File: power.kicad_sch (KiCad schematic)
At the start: 19 parts, among them J7 Input, U1 U

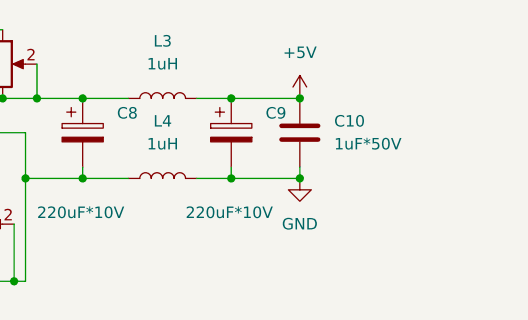
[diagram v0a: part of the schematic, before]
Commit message: Fix errors with LCD connection
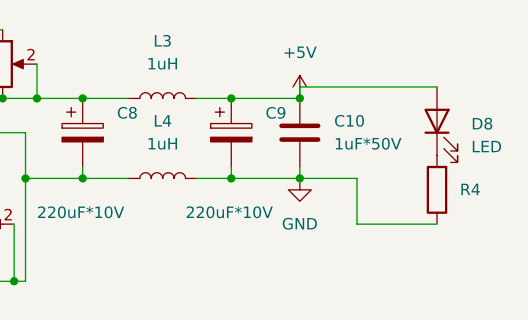
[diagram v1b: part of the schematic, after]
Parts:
- added D8: LED, LED_THT:LED_D3.0mm, symbol Device:LED
- added R4: 330, Resistor_SMD:R_1206_3216Metric_Pad1.30x1.75mm_HandSolder, symbol Device:R
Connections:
- net +5V: now also D8.2 (A)
- net GND: now also R4.1
- new net: D8.1 (K), R4.2
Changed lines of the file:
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@@
+	(wire
+		(pts
+			(xy 251.46 50.8) (xy 251.46 52.07)
+		)
+		(stroke
+			(width 0)
+			(type default)
+		)
+	)
 	(wire
 		(pts
@@
 	(wire
 		(pts
+			(xy 257.81 66.04) (xy 257.81 60.96)
+		)
+		(stroke
+			(width 0)
+			(type default)
+		)
+	)
+	(wire
+		(pts
 			(xy 222.25 48.26) (xy 222.25 52.07)
 		)
@@
 	(wire
 		(pts
+			(xy 257.81 60.96) (xy 251.46 60.96)
+		)
+		(stroke
+			(width 0)
+			(type default)
+		)
+	)
+	(wire
+		(pts
 			(xy 29.21 53.34) (xy 26.67 53.34)
 		)
@@
 	(wire
 		(pts
+			(xy 266.7 66.04) (xy 257.81 66.04)
+		)
+		(stroke
+			(width 0)
+			(type default)
+		)
+	)
+	(wire
+		(pts
 			(xy 243.84 52.07) (xy 251.46 52.07)
 		)
@@
 		(pts
 			(xy 29.21 63.5) (xy 29.21 53.34)
+		)
+		(stroke
+			(width 0)
+			(type default)
+		)
+	)
+	(wire
+		(pts
+			(xy 266.7 50.8) (xy 251.46 50.8)
 		)
 		(stroke
@@
 	)
 	(symbol
+		(lib_id "Device:LED")
+		(at 266.7 54.61 90)
+		(unit 1)
+		(exclude_from_sim no)
+		(in_bom yes)
+		(on_board yes)
+		(dnp no)
+		(fields_autoplaced yes)
+		(property "Reference" "D8"
+			(at 270.51 54.9274 90)
+			(effects
+				(font
+					(size 1.27 1.27)
+				)
+				(justify right)
+			)
+		)
+		(property "Value" "LED"
+			(at 270.51 57.4674 90)
+			(effects
+				(font
+					(size 1.27 1.27)
+				)
+				(justify right)
+			)
+		)
+		(property "Footprint" "LED_THT:LED_D3.0mm"
+			(at 266.7 54.61 0)
+			(effects
+				(font
+					(size 1.27 1.27)
+				)
+				(hide yes)
+			)
+		)
+		(property "Datasheet" "~"
+			(at 266.7 54.61 0)
+			(effects
+				(font
+					(size 1.27 1.27)
+				)
+				(hide yes)
+			)
+		)
+		(property "Description" "Light emitting diode"
+			(at 266.7 54.61 0)
+			(effects
+				(font
+					(size 1.27 1.27)
+				)
+				(hide yes)
+			)
+		)
+		(pin "1"
+		)
+		(pin "2"
+		)
+		(instances
+			(project "fpga_board"
+				(path "/7e985ab5-4049-4d72-94c7-921d31b1011c/03a43814-5da6-4596-9846-af885616fedd"
+					(reference "D8")
+					(unit 1)
+				)
+			)
+		)
+	)
+	(symbol
 		(lib_id "Device:R_Potentiometer")
 		(at 215.9 66.04 0)
@@
 					(unit 1)
 				)
+			)
+		)
+	)
+	(symbol
+		(lib_id "Device:R")
+		(at 266.7 62.23 180)
+		(unit 1)
+		(exclude_from_sim no)
+		(in_bom yes)
+		(on_board yes)
+		(dnp no)
+		(fields_autoplaced yes)
+		(property "Reference" "R4"
+			(at 269.24 62.2299 0)
+			(effects
+				(font
+					(size 1.27 1.27)
+				)
+				(justify right)
+			)
+		)
+		(property "Value" "330"
+			(at 262.89 62.23 90)
+			(effects
+				(font
+					(size 1.27 1.27)
+				)
+				(hide yes)
+			)
+		)
+		(property "Footprint" "Resistor_SMD:R_1206_3216Metric_Pad1.30x1.75mm_HandSolder"
+			(at 268.478 62.23 90)
+			(effects
+				(font
+					(size 1.27 1.27)
+				)
+				(hide yes)
+			)
+		)
+		(property "Datasheet" "~"
+			(at 266.7 62.23 0)
+			(effects
+				(font
+					(size 1.27 1.27)
+				)
+				(hide yes)
+			)
+		)
+		(property "Description" "Resistor"
+			(at 266.7 62.23 0)
+			(effects
+				(font
+					(size 1.27 1.27)
+				)
+				(hide yes)
+			)
+		)
+		(pin "1"
+		)
+		(pin "2"
+		)
+		(instances
+			(project "fpga_board"
+				(path "/7e985ab5-4049-4d72-94c7-921d31b1011c/03a43814-5da6-4596-9846-af885616fedd"
+					(reference "R4")
+					(unit 1)
+				)

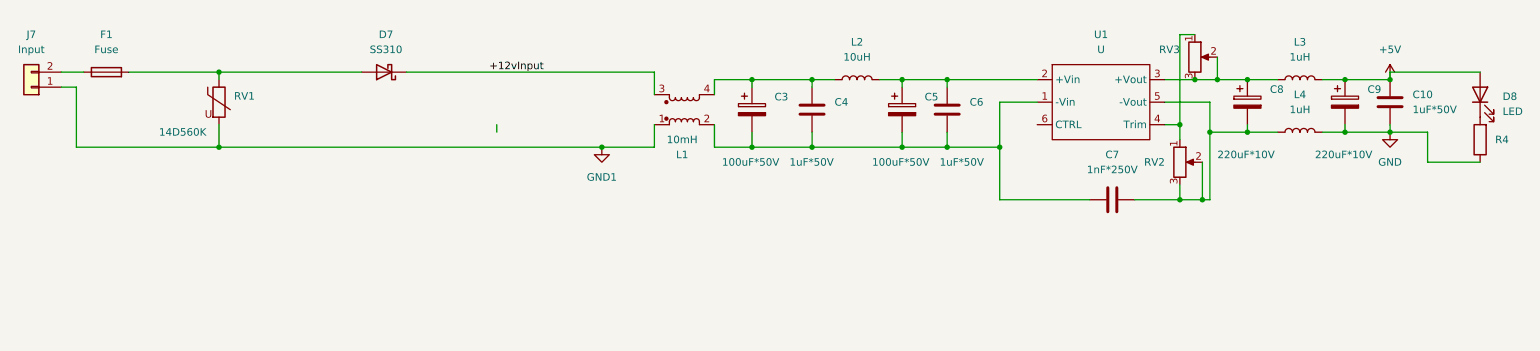
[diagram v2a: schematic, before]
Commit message: Make 3d model for ADC and FPGA. Trying to assembly
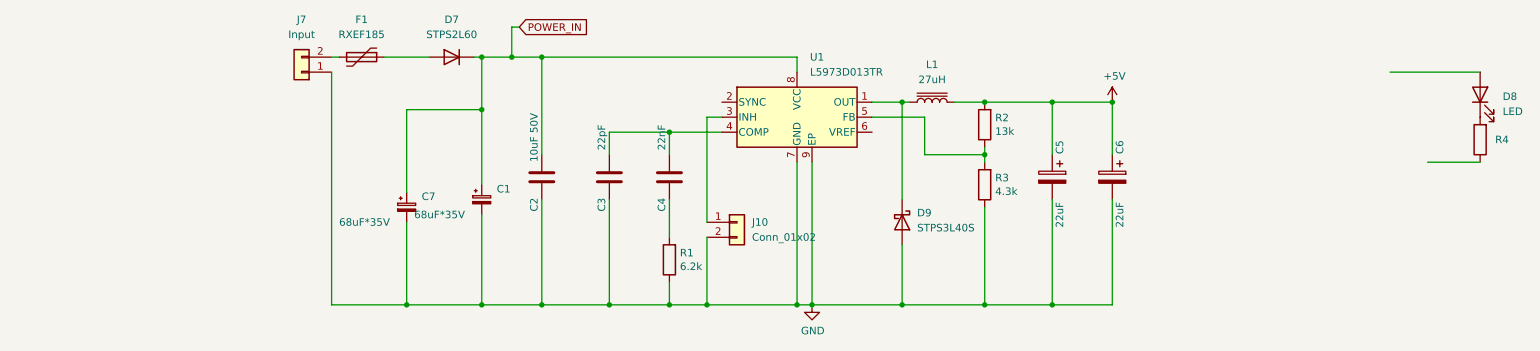
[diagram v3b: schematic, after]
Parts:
- removed C10, C6: 1uF*50V, Capacitor_SMD:C_1206_3216Metric_Pad1.33x1.80mm_HandSolder, symbol Device:C
- removed C3: 100uF*50V, Capacitor_THT:CP_Radial_D8.0mm_P3.50mm, symbol Device:C_Polarized
- removed C7: 1nF*250V, Capacitor_SMD:C_1206_3216Metric_Pad1.33x1.80mm_HandSolder, symbol Device:C
- removed C8, C9: 220uF*10V, Capacitor_THT:CP_Radial_D6.3mm_P2.50mm, symbol Device:C_Polarized
- removed D7: SS310, Diode_SMD:D_SMA, symbol Diode:SS310
- removed F1: Fuse, Resistor_THT:R_Axial_DIN0309_L9.0mm_D3.2mm_P12.70mm_Horizontal, symbol Device:Fuse
- removed L1: 10mH, PowerLibrary:IndRing, symbol Device:L_Coupled
- removed L2: 10uH, Inductor_SMD:L_6.3x6.3_H3, symbol Device:L
- removed L3, L4: 1uH, Inductor_SMD:L_6.3x6.3_H3, symbol Device:L
- removed RV1: 14D560K, eec:Bourns_Inc.-MOV-14D471K-MFG, symbol Device:Varistor
- removed RV2, RV3: R_Potentiometer, DPAK:TRIM_3296W-1-203, symbol Device:R_Potentiometer
- removed U1: U, PowerLibrary:HLK, symbol powermod:U
- added C1, C7: 68uF*35V, Capacitor_Tantalum_SMD:CP_EIA-7361-38_AVX-V_Pad2.18x3.30mm_HandSolder, symbol Device:C_Polarized_Small
- added C2: 10uF 50V, Capacitor_SMD:C_1210_3225Metric_Pad1.33x2.70mm_HandSolder, symbol Device:C
- added C3: 22pF, Capacitor_SMD:C_0805_2012Metric_Pad1.18x1.45mm_HandSolder, symbol Device:C
- added C6: 22uF, Capacitor_Tantalum_SMD:CP_EIA-3528-21_Kemet-B_Pad1.50x2.35mm_HandSolder, symbol Device:C_Polarized
- added D7: STPS2L60, Diode_SMD:D_SMA, symbol Diode:1N914
- added D9: STPS3L40S, Diode_SMD:D_SMC, symbol Diode:1N6857UR
- added F1: RXEF185, Fuse:CAPRB1000W55L1500T500H1900, symbol Device:Polyfuse
- added J10: Conn_01x02, Connector_PinHeader_2.00mm:PinHeader_1x02_P2.00mm_Vertical, symbol Connector_Generic:Conn_01x02
- added L1: 27uH, Inductor_SMD:L_Bourns_SRR1208_12.7x12.7mm, symbol Device:L_Iron
- added R1: 6.2k, Resistor_SMD:R_0805_2012Metric_Pad1.20x1.40mm_HandSolder, symbol Device:R
- added R2: 13k, Resistor_SMD:R_0805_2012Metric_Pad1.20x1.40mm_HandSolder, symbol Device:R
- added R3: 4.3k, Resistor_SMD:R_0805_2012Metric_Pad1.20x1.40mm_HandSolder, symbol Device:R
- added U1: L5973D013TR, Package_SO:HSOP-8-1EP_3.9x4.9mm_P1.27mm_EP2.41x3.1mm_ThermalVias, symbol Regulator_Switching:L5973D
- C4: value 1uF*50V -> 22nF; footprint Capacitor_SMD:C_1206_3216Metric_Pad1.33x1.80mm_HandSolder -> Capacitor_SMD:C_0805_2012Metric_Pad1.18x1.45mm_HandSolder; Field4 https://radiocom-vn.prom.ua/ua/p1156592486-mkf-y5v-50v.html -> (none)
- C5: value 100uF*50V -> 22uF; footprint Capacitor_THT:CP_Radial_D8.0mm_P3.50mm -> Capacitor_Tantalum_SMD:CP_EIA-3528-21_Kemet-B_Pad1.50x2.35mm_HandSolder; Field4 https://radiocom-vn.prom.ua/ua/p1156596165-100mkf-50v-capxs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 -> (none)
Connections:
- net GND1 is gone; now on net GND: J7.1 (Pin_1)
- net +5V: now also C5.1, C6.1, L1.2, R2.2; no longer D8.2 (A)
- net GND: now also C5.2, C1.2, C2.2, C3.2, C6.2, C7.2, D9.2 (A), J10.2 (Pin_2), R1.1, R3.1, U1.7 (GND), U1.9 (EP); no longer R4.1
- net at C4.1: now also C3.1, U1.4 (COMP)
- net at C4.2: now also R1.2; no longer C5.2
- net at J7.2 (Pin_2): now also F1.2
- new net: D9.1 (K), L1.1, U1.1 (OUT)
- new net: R2.1, R3.2, U1.5 (FB)
- new net: D7.2 (A), F1.1
- new net: J10.1 (Pin_1), U1.3 (INH)
- new net POWER_IN: C1.1, C2.1, C7.1, D7.1 (K), U1.8 (VCC)
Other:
- moved on the sheet: J7
